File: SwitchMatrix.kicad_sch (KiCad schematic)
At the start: 160 parts, among them SW1 1u, SW10 1u, SW11 1u, SW12 1u, SW13 1u, SW14 1u, SW15 1u, SW16 1u, SW17 2u, SW18 1.5u, SW19 1u, SW2 1u, SW20 1u, SW21 1u, SW22 1u, SW23 1u, SW24 1u, SW25 1u, SW26 1u, SW27 1u, SW28 1u, SW29 1u, SW3 1u, SW30 1u, SW31 1.5u, SW32 ISO Enter, SW33 1u, SW34 1.25u, SW35 1.75u, SW36 1u, SW37 1u, SW38 1u, SW39 1u, SW4 1u, SW40 1u, SW41 1u, SW42 1u, SW43 1u, SW44 1u, SW45 1u, SW46 1u, SW47 2.25u, SW48 1u, SW49 1u, SW5 1u, SW50 2.25u, SW51 1.25u, SW52 1u, SW53 1u, SW54 1u, SW55 1u, SW56 1u, SW57 1u, SW58 1u, SW59 1u, SW6 1u, SW60 1u, SW61 1u, SW62 1u, SW63 1.75u, SW64 1u, SW65 1u, SW66 1.5u, SW67 1.25u, SW68 1u, SW69 1.25u, SW7 1u, SW70 1.5u, SW71 1.25u, SW72 3u, SW73 7u, SW74 6.25u, SW75 3u, SW76 1.25u, SW77 1.5u, SW78 1.25u, SW79 1u, SW8 1u, SW80 1u, SW81 1u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

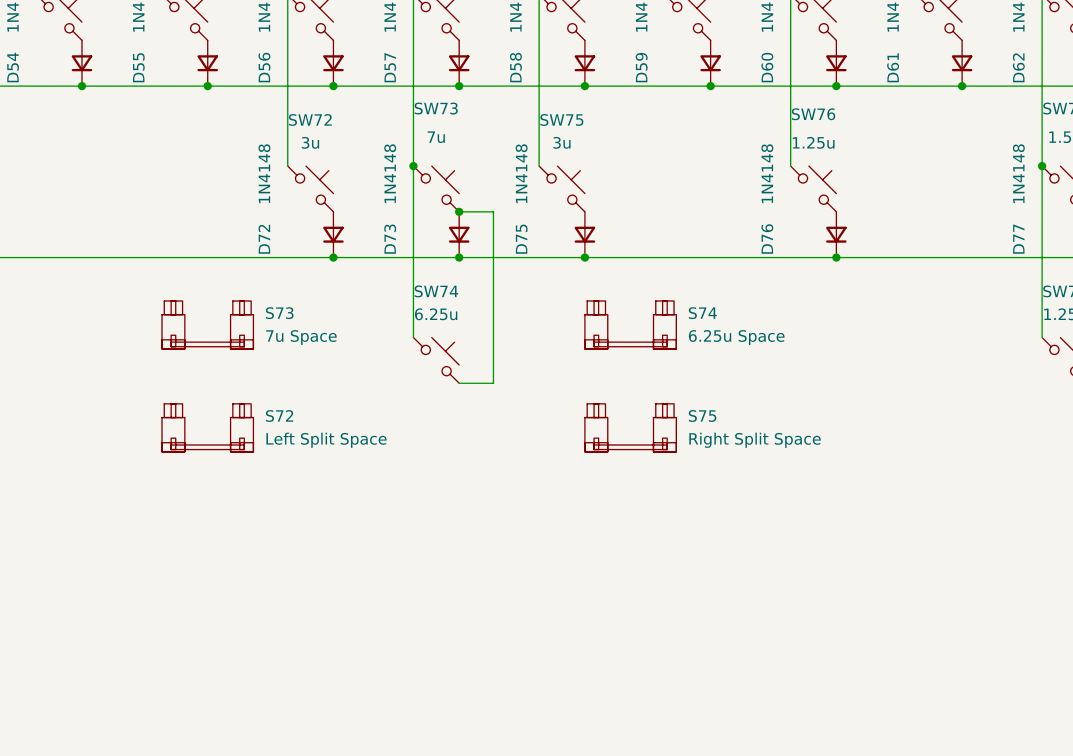
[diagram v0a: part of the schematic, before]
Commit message: Polyfuse and 2u split space
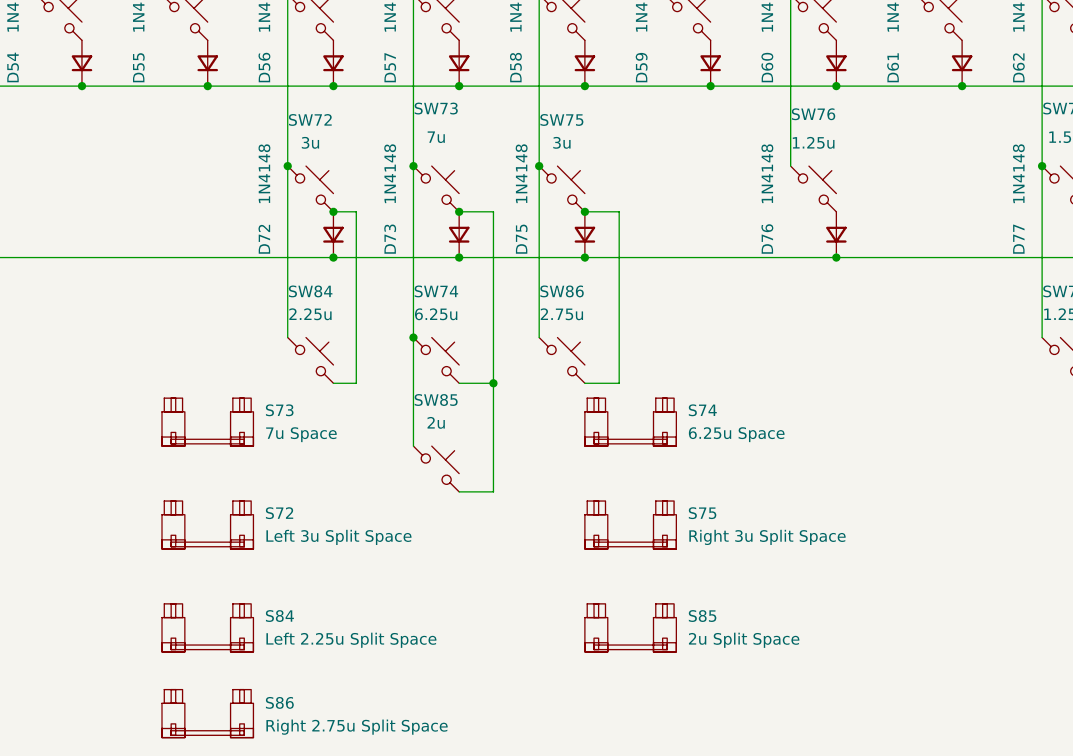
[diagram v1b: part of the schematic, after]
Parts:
- added S84: Left 2.25u Split Space, marbastlib-mx:STAB_MX_P_6.25u, symbol marbastlib-mx:MX_stab
- added S85: 2u Split Space, marbastlib-mx:STAB_MX_P_6.25u, symbol marbastlib-mx:MX_stab
- added S86: Right 2.75u Split Space, marbastlib-mx:STAB_MX_P_6.25u, symbol marbastlib-mx:MX_stab
- added SW84: 2.25u, marbastlib-mx:SW_MX_1u, symbol marbastlib-mx:MX_SW_solder
- added SW85: 2u, marbastlib-mx:SW_MX_1u, symbol marbastlib-mx:MX_SW_solder
- added SW86: 2.75u, marbastlib-mx:SW_MX_1u, symbol marbastlib-mx:MX_SW_solder
- S72: value Left Split Space -> Left 3u Split Space
- S75: value Right Split Space -> Right 3u Split Space
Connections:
- net COL5: now also SW84.1
- net COL6: now also SW85.1
- net COL7: now also SW86.1
- net at D73.2 (A), SW73.2, SW74.2: now also SW85.2
- net at D72.2 (A), SW72.2: now also SW84.2
- net at D75.2 (A), SW75.2: now also SW86.2
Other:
- moved on the sheet: S72, S73, S74, S75

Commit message: Assign footprints (again)
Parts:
- S47: footprint marbastlib-mx:STAB_MX_P_2.25u -> marbastlib-mx:STAB_MX_2.25u
- S72, S75: footprint marbastlib-mx:STAB_MX_P_3u -> marbastlib-mx:STAB_MX_3u
- S73: footprint marbastlib-mx:STAB_MX_P_7u -> marbastlib-mx:STAB_MX_7u
- S74: footprint marbastlib-mx:STAB_MX_P_6.25u -> marbastlib-mx:STAB_MX_6.25u
- S84: footprint marbastlib-mx:STAB_MX_P_6.25u -> marbastlib-mx:STAB_MX_2.25u
- S85: footprint marbastlib-mx:STAB_MX_P_6.25u -> marbastlib-mx:STAB_MX_2u
- S86: footprint marbastlib-mx:STAB_MX_P_6.25u -> marbastlib-mx:STAB_MX_2.75u
- SW18, SW31, SW66, SW70, SW77: footprint marbastlib-mx:SW_MX_1u -> marbastlib-mx:SW_MX_1.5u
- SW34, SW51, SW67, SW69, SW71, SW76, SW78: footprint marbastlib-mx:SW_MX_1u -> marbastlib-mx:SW_MX_1.25u
- SW35, SW63: footprint marbastlib-mx:SW_MX_1u -> marbastlib-mx:SW_MX_1.75u
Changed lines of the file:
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@@
     (property "Reference" "SW18" (id 0) (at 44.45 67.31 0))
     (property "Value" "1.5u" (id 1) (at 44.45 69.85 0))
-    (property "Footprint" "marbastlib-mx:SW_MX_1u" (id 2) (at 44.45 74.93 0)
+    (property "Footprint" "marbastlib-mx:SW_MX_1.5u" (id 2) (at 44.45 74.93 0)
       (effects (font (size 1.27 1.27)) hide)
     )
@@
     (property "Reference" "SW67" (id 0) (at 44.45 142.24 0))
     (property "Value" "1.25u" (id 1) (at 44.45 144.78 0))
-    (property "Footprint" "marbastlib-mx:SW_MX_1u" (id 2) (at 44.45 149.86 0)
+    (property "Footprint" "marbastlib-mx:SW_MX_1.25u" (id 2) (at 44.45 149.86 0)
       (effects (font (size 1.27 1.27)) hide)
     )
@@
     (property "Reference" "SW35" (id 0) (at 44.45 85.09 0))
     (property "Value" "1.75u" (id 1) (at 44.45 87.63 0))
-    (property "Footprint" "marbastlib-mx:SW_MX_1u" (id 2) (at 44.45 92.71 0)
+    (property "Footprint" "marbastlib-mx:SW_MX_1.75u" (id 2) (at 44.45 92.71 0)
       (effects (font (size 1.27 1.27)) hide)
     )
@@
     (property "Reference" "SW66" (id 0) (at 44.45 121.92 0))
     (property "Value" "1.5u" (id 1) (at 44.45 125.095 0))
-    (property "Footprint" "marbastlib-mx:SW_MX_1u" (id 2) (at 44.45 130.81 0)
+    (property "Footprint" "marbastlib-mx:SW_MX_1.5u" (id 2) (at 44.45 130.81 0)
       (effects (font (size 1.27 1.27)) hide)
     )
@@
     (property "Reference" "SW71" (id 0) (at 72.39 142.24 0))
     (property "Value" "1.25u" (id 1) (at 72.39 144.78 0))
-    (property "Footprint" "marbastlib-mx:SW_MX_1u" (id 2) (at 72.39 149.86 0)
+    (property "Footprint" "marbastlib-mx:SW_MX_1.25u" (id 2) (at 72.39 149.86 0)
       (effects (font (size 1.27 1.27)) hide)
     )
@@
       (effects (font (size 1.27 1.27)) (justify left))
     )
-    (property "Footprint" "marbastlib-mx:STAB_MX_P_3u" (id 2) (at 149.86 168.275 0)
+    (property "Footprint" "marbastlib-mx:STAB_MX_3u" (id 2) (at 149.86 168.275 0)
       (effects (font (size 1.27 1.27)) hide)
     )
@@
     (property "Reference" "SW31" (id 0) (at 226.06 67.31 0))
     (property "Value" "1.5u" (id 1) (at 226.06 69.85 0))
-    (property "Footprint" "marbastlib-mx:SW_MX_1u" (id 2) (at 226.06 74.93 0)
+    (property "Footprint" "marbastlib-mx:SW_MX_1.5u" (id 2) (at 226.06 74.93 0)
       (effects (font (size 1.27 1.27)) hide)
     )
@@
     (property "Reference" "SW51" (id 0) (at 44.45 104.14 0))
     (property "Value" "1.25u" (id 1) (at 44.45 106.68 0))
-    (property "Footprint" "marbastlib-mx:SW_MX_1u" (id 2) (at 44.45 111.76 0)
+    (property "Footprint" "marbastlib-mx:SW_MX_1.25u" (id 2) (at 44.45 111.76 0)
       (effects (font (size 1.27 1.27)) hide)
     )
@@
       (effects (font (size 1.27 1.27)) (justify left))
     )
-    (property "Footprint" "marbastlib-mx:STAB_MX_P_6.25u" (id 2) (at 102.87 179.705 0)
+    (property "Footprint" "marbastlib-mx:STAB_MX_2.25u" (id 2) (at 102.87 179.705 0)
       (effects (font (size 1.27 1.27)) hide)
     )
@@
       (effects (font (size 1.27 1.27)) (justify left))
     )
-    (property "Footprint" "marbastlib-mx:STAB_MX_P_6.25u" (id 2) (at 149.86 156.845 0)
+    (property "Footprint" "marbastlib-mx:STAB_MX_6.25u" (id 2) (at 149.86 156.845 0)
       (effects (font (size 1.27 1.27)) hide)
     )
@@
     (property "Reference" "SW76" (id 0) (at 170.18 122.555 0))
     (property "Value" "1.25u" (id 1) (at 170.18 125.73 0))
-    (property "Footprint" "marbastlib-mx:SW_MX_1u" (id 2) (at 170.18 130.81 0)
+    (property "Footprint" "marbastlib-mx:SW_MX_1.25u" (id 2) (at 170.18 130.81 0)
       (effects (font (size 1.27 1.27)) hide)
     )
@@
       (effects (font (size 1.27 1.27)) (justify left))
     )
-    (property "Footprint" "marbastlib-mx:STAB_MX_P_7u" (id 2) (at 102.87 156.845 0)
+    (property "Footprint" "marbastlib-mx:STAB_MX_7u" (id 2) (at 102.87 156.845 0)
       (effects (font (size 1.27 1.27)) hide)
     )
@@
     (property "Reference" "SW77" (id 0) (at 198.12 121.92 0))
     (property "Value" "1.5u" (id 1) (at 198.12 125.095 0))
-    (property "Footprint" "marbastlib-mx:SW_MX_1u" (id 2) (at 198.12 130.81 0)
+    (property "Footprint" "marbastlib-mx:SW_MX_1.5u" (id 2) (at 198.12 130.81 0)
       (effects (font (size 1.27 1.27)) hide)
     )
@@
       (effects (font (size 1.27 1.27)) (justify left))
     )
-    (property "Footprint" "marbastlib-mx:STAB_MX_P_6.25u" (id 2) (at 149.86 179.705 0)
+    (property "Footprint" "marbastlib-mx:STAB_MX_2u" (id 2) (at 149.86 179.705 0)
       (effects (font (size 1.27 1.27)) hide)
     )
@@
     (property "Reference" "SW34" (id 0) (at 29.21 85.09 0))
     (property "Value" "1.25u" (id 1) (at 29.21 87.63 0))
-    (property "Footprint" "marbastlib-mx:SW_MX_1u" (id 2) (at 29.21 92.71 0)
+    (property "Footprint" "marbastlib-mx:SW_MX_1.25u" (id 2) (at 29.21 92.71 0)
       (effects (font (size 1.27 1.27)) hide)
     )
@@
     (property "Reference" "SW63" (id 0) (at 212.09 104.14 0))
     (property "Value" "1.75u" (id 1) (at 212.09 106.68 0))
-    (property "Footprint" "marbastlib-mx:SW_MX_1u" (id 2) (at 212.09 111.76 0)
+    (property "Footprint" "marbastlib-mx:SW_MX_1.75u" (id 2) (at 212.09 111.76 0)
       (effects (font (size 1.27 1.27)) hide)
     )
@@
     (property "Reference" "SW70" (id 0) (at 72.39 121.92 0))
     (property "Value" "1.5u" (id 1) (at 72.39 125.095 0))
-    (property "Footprint" "marbastlib-mx:SW_MX_1u" (id 2) (at 72.39 130.81 0)
+    (property "Footprint" "marbastlib-mx:SW_MX_1.5u" (id 2) (at 72.39 130.81 0)
       (effects (font (size 1.27 1.27)) hide)
     )
@@
     (property "Reference" "SW78" (id 0) (at 198.12 142.24 0))
     (property "Value" "1.25u" (id 1) (at 198.12 144.78 0))
-    (property "Footprint" "marbastlib-mx:SW_MX_1u" (id 2) (at 198.12 149.86 0)
+    (property "Footprint" "marbastlib-mx:SW_MX_1.25u" (id 2) (at 198.12 149.86 0)
       (effects (font (size 1.27 1.27)) hide)
     )
@@
       (effects (font (size 1.27 1.27)) (justify left))
     )
-    (property "Footprint" "marbastlib-mx:STAB_MX_P_3u" (id 2) (at 102.87 168.275 0)
+    (property "Footprint" "marbastlib-mx:STAB_MX_3u" (id 2) (at 102.87 168.275 0)
       (effects (font (size 1.27 1.27)) hide)
     )
@@
     (property "Reference" "SW69" (id 0) (at 58.42 142.24 0))
     (property "Value" "1.25u" (id 1) (at 58.42 144.78 0))
-    (property "Footprint" "marbastlib-mx:SW_MX_1u" (id 2) (at 58.42 149.86 0)
+    (property "Footprint" "marbastlib-mx:SW_MX_1.25u" (id 2) (at 58.42 149.86 0)
       (effects (font (size 1.27 1.27)) hide)
     )
@@
       (effects (font (size 1.27 1.27)) (justify left))
     )
-    (property "Footprint" "marbastlib-mx:STAB_MX_P_6.25u" (id 2) (at 102.87 189.23 0)
+    (property "Footprint" "marbastlib-mx:STAB_MX_2.75u" (id 2) (at 102.87 189.23 0)
       (effects (font (size 1.27 1.27)) hide)
     )
@@
       (effects (font (size 1.27 1.27)) (justify right))
     )
-    (property "Footprint" "marbastlib-mx:STAB_MX_P_2.25u" (id 2) (at 265.43 88.9 0)
-      (effects (font (size 1.27 1.27)) hide)
-    )
+    (property "Footprint" "marbastlib-mx:STAB_MX_2.25u" (id 2) (at 265.43 88.9 0)
+      (effects (font (size 1.27 1.27)) hide)
+    )

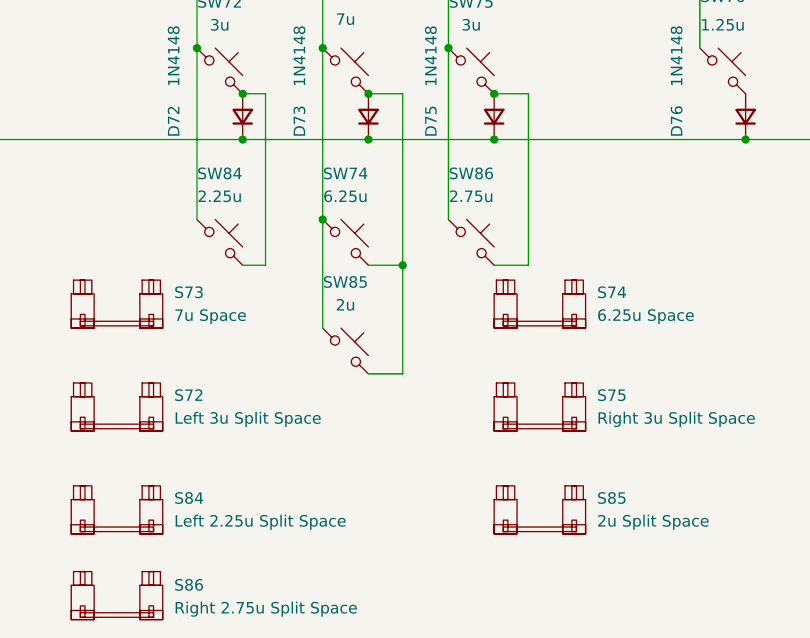
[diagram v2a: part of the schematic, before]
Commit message: Place switches (with broken stabs)
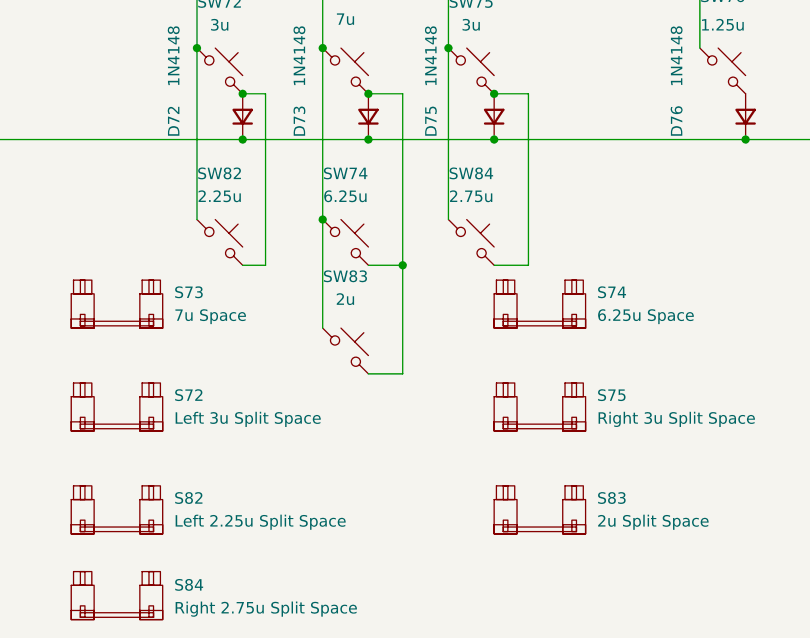
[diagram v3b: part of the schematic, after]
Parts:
- renumbered S84 to S82, S85 to S83, S86 to S84, SW84 to SW82, SW85 to SW83, SW86 to SW84
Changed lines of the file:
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@@
   (symbol (lib_id "marbastlib-mx:MX_SW_solder") (at 128.27 161.925 0) (unit 1)
     (in_bom yes) (on_board yes) (fields_autoplaced)
-    (property "Reference" "SW85" (id 0) (at 128.27 154.305 0))
-    (property "Value" "2u" (id 1) (at 128.27 156.845 0))
+    (property "Reference" "SW83" (id 0) (at 128.27 153.67 0))
+    (property "Value" "2u" (id 1) (at 128.27 156.21 0))
     (property "Footprint" "marbastlib-mx:SW_MX_1u" (id 2) (at 128.27 161.925 0)
       (effects (font (size 1.27 1.27)) hide)
@@
   (symbol (lib_id "marbastlib-mx:MX_stab") (at 102.87 179.705 0) (unit 1)
     (in_bom yes) (on_board yes) (fields_autoplaced)
-    (property "Reference" "S84" (id 0) (at 109.22 178.3079 0)
+    (property "Reference" "S82" (id 0) (at 109.22 178.3079 0)
       (effects (font (size 1.27 1.27)) (justify left))
     )
@@
   (symbol (lib_id "marbastlib-mx:MX_stab") (at 149.86 179.705 0) (unit 1)
     (in_bom yes) (on_board yes) (fields_autoplaced)
-    (property "Reference" "S85" (id 0) (at 156.21 178.3079 0)
+    (property "Reference" "S83" (id 0) (at 156.21 178.3079 0)
       (effects (font (size 1.27 1.27)) (justify left))
     )
@@
   (symbol (lib_id "marbastlib-mx:MX_SW_solder") (at 114.3 149.86 0) (unit 1)
     (in_bom yes) (on_board yes) (fields_autoplaced)
-    (property "Reference" "SW84" (id 0) (at 114.3 142.24 0))
+    (property "Reference" "SW82" (id 0) (at 114.3 142.24 0))
     (property "Value" "2.25u" (id 1) (at 114.3 144.78 0))
     (property "Footprint" "marbastlib-mx:SW_MX_1u" (id 2) (at 114.3 149.86 0)
@@
   (symbol (lib_id "marbastlib-mx:MX_SW_solder") (at 142.24 149.86 0) (unit 1)
     (in_bom yes) (on_board yes) (fields_autoplaced)
-    (property "Reference" "SW86" (id 0) (at 142.24 142.24 0))
+    (property "Reference" "SW84" (id 0) (at 142.24 142.24 0))
     (property "Value" "2.75u" (id 1) (at 142.24 144.78 0))
     (property "Footprint" "marbastlib-mx:SW_MX_1u" (id 2) (at 142.24 149.86 0)
@@
   (symbol (lib_id "marbastlib-mx:MX_stab") (at 102.87 189.23 0) (unit 1)
     (in_bom yes) (on_board yes)
-    (property "Reference" "S86" (id 0) (at 109.22 187.96 0)
+    (property "Reference" "S84" (id 0) (at 109.22 187.96 0)
       (effects (font (size 1.27 1.27)) (justify left))
     )

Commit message: Attempt to get stabs to work
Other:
- moved on the sheet: S47
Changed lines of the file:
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@@
     (pin "2")
   )
-  (symbol (lib_id "marbastlib-mx:MX_stab") (at 265.43 88.9 90) (unit 1)
-    (in_bom yes) (on_board yes) (fields_autoplaced)
-    (property "Reference" "S47" (id 0) (at 269.24 87.6299 90)
+  (symbol (lib_id "marbastlib-mx:MX_stab") (at 215.265 91.44 90) (unit 1)
+    (in_bom yes) (on_board yes)
+    (property "Reference" "S47" (id 0) (at 213.36 85.09 90)
       (effects (font (size 1.27 1.27)) (justify right))
     )
-    (property "Value" "Enter" (id 1) (at 269.24 90.1699 90)
+    (property "Value" "Enter" (id 1) (at 211.455 90.17 90)
       (effects (font (size 1.27 1.27)) (justify right))
     )
-    (property "Footprint" "marbastlib-mx:STAB_MX_2.25u" (id 2) (at 265.43 88.9 0)
+    (property "Footprint" "marbastlib-mx:STAB_MX_2.25u" (id 2) (at 215.265 91.44 0)
       (effects (font (size 1.27 1.27)) hide)
     )
-    (property "Datasheet" "" (id 3) (at 265.43 88.9 0)
+    (property "Datasheet" "" (id 3) (at 215.265 91.44 0)
       (effects (font (size 1.27 1.27)) hide)
     )
